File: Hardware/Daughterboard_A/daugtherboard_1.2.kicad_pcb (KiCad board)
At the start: 2 copper layers, 165.6 x 82.3 mm, 72 parts, among them J2 RJ45, J3 RJ45, J4 Conn_01x07, J5 Conn_01x04, J6 Conn_01x07, U1 IM66D132H, U16 TXS0108EPW, U17 LP5907MFX-1.8/NOPB, U2 IM66D132H, U3 IM66D132H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

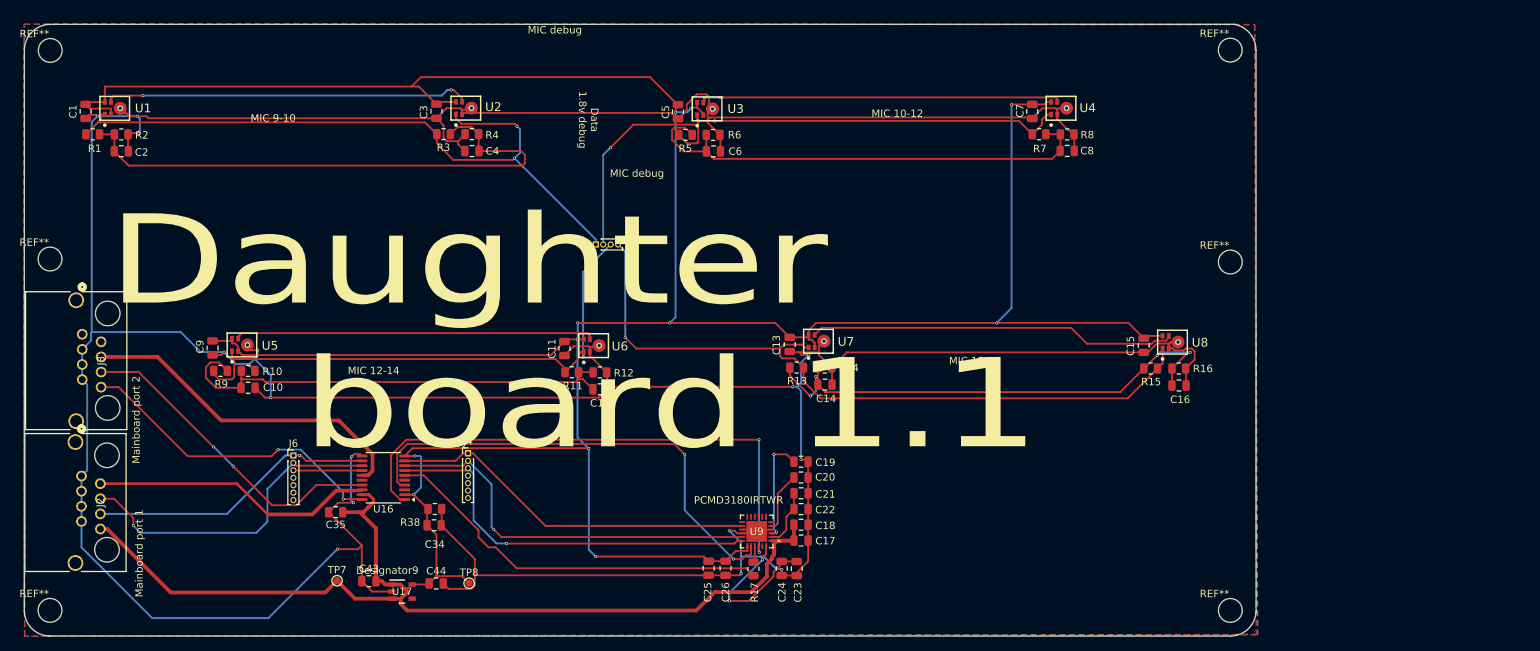
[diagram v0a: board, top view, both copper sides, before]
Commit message: implemented  ethernet port pcb R/a
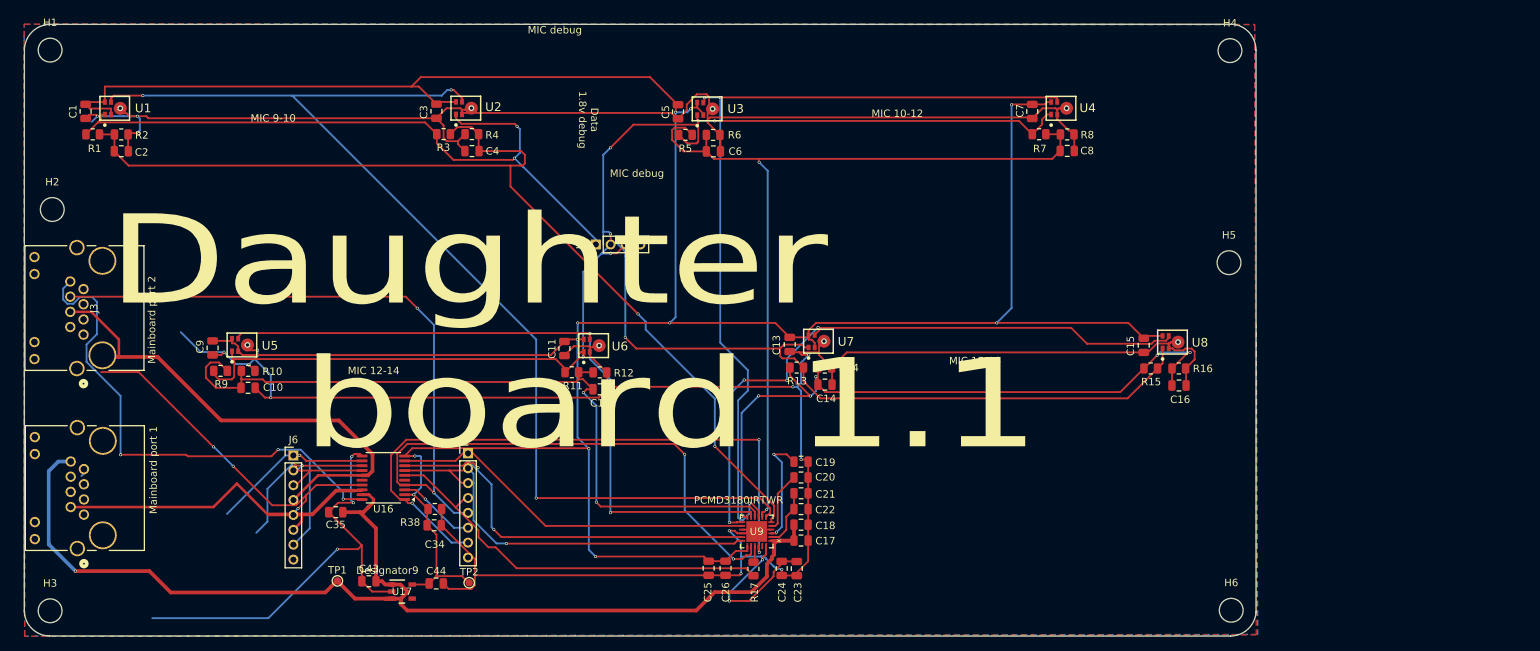
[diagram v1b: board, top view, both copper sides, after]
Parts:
- removed REF** (x6): MountingHole_3.2mm_M3, MountingHole:MountingHole_3.2mm_M3
- removed TP7, TP8: TestPoint, TestPoint:TestPoint_Pad_D1.0mm
- added H1: 3.2mm, MountingHole:MountingHole_3.2mm_M3_ISO14580, F.Cu at (46.8, 36.6)
- added H2: 3.2mm, MountingHole:MountingHole_3.2mm_M3_ISO14580, F.Cu at (47.0, 58.1)
- added H3: 3.2mm, MountingHole:MountingHole_3.2mm_M3_ISO14580, F.Cu at (46.8, 112.0)
- added H4: 3.2mm, MountingHole:MountingHole_3.2mm_M3_ISO14580, F.Cu at (205.4, 36.7)
- added H5: 3.2mm, MountingHole:MountingHole_3.2mm_M3_ISO14580, F.Cu at (205.2, 65.2)
- added H6: 3.2mm, MountingHole:MountingHole_3.2mm_M3_ISO14580, F.Cu at (205.6, 111.9)
- added TP1: TestPoint, TestPoint:TestPoint_Pad_D1.0mm, F.Cu at (85.4, 108.0)
- added TP2: TestPoint, TestPoint:TestPoint_Pad_D1.0mm, F.Cu at (103.1, 108.2)
- J2, J3: value RJ45 -> RJHSE5380; footprint RJHSE-3380:CONN_RJHSE-3380_AMP -> RJHSE-5380:RJHSE5380_AMP
- J4, J6: value Conn_01x07 -> Conn_01x08; footprint Connector_PinHeader_1.00mm:PinHeader_1x07_P1.00mm_Vertical -> Connector_PinHeader_2.00mm:PinHeader_1x08_P2.00mm_Vertical
- J5: footprint Connector_PinHeader_1.00mm:PinHeader_1x04_P1.00mm_Vertical -> Connector_PinHeader_2.00mm:PinHeader_1x04_P2.00mm_Vertical
- moved J2 1.61 mm to (51.4, 95.5)
- moved J3 0.18 mm to (51.2, 74.9)
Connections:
- C10 pad 1: micGRP_3out_1.8V -> micGRP_7out_1.8V
- C12 pad 1: micGRP_3out_1.8V -> micGRP_7out_1.8V
- C14 pad 1: micGRP_4out_1.8V -> micGRP_8out_1.8V
- C16 pad 1: micGRP_4out_1.8V -> micGRP_8out_1.8V
- C2 pad 1: micGRP_1out_1.8V -> micGRP_5out_1.8V
- C4 pad 1: micGRP_1out_1.8V -> micGRP_5out_1.8V
- C6 pad 1: micGRP_2out_1.8V -> micGRP_6out_1.8V
- C8 pad 1: micGRP_2out_1.8V -> micGRP_6out_1.8V
- J2 pad 10: (no net) -> GND
- J2 pad 9: (no net) -> unconnected-(J2-Pad9)
- J3 pad 1: unconnected-(J3-Pad1) -> GND
- J3 pad 10: (no net) -> GND
- J3 pad 2: unconnected-(J3-Pad2) -> SDA_SSZ_1.8V
- J3 pad 6: MCLK_TDM2_3.3V -> MCLK_TDM2_1.8V
- J3 pad 9: (no net) -> GND
- J4 pad 4: OUTPUT_TDM1_1.8V -> OUTPUT_TDM2_1.8V
- J4 pad 5: MCLK_TDM1_1.8V -> MCLK_TDM2_1.8V
- J4 pad 6: FSYNC_TDM1_1.8V -> FSYNC_TDM2_1.8V
- J4 pad 7: BCLK_TDM1_1.8V -> BCLK_TDM2_1.8V
- J6 pad 4: OUTPUT_TDM1_3.3V -> OUTPUT_TDM2_3.3V
- J6 pad 5: MCLK_TDM1_3.3V -> MCLK_TDM2_3.3V
- J6 pad 6: FSYNC_TDM1_3.3V -> FSYNC_TDM2_3.3V
- J6 pad 7: BCLK_TDM1_3.3V -> BCLK_TDM2_3.3V
- R1 pad 2: micGRP_1out_1.8V -> micGRP_5out_1.8V
- R10 pad 1: micGRP_3out_1.8V -> micGRP_7out_1.8V
- R11 pad 2: micGRP_3out_1.8V -> micGRP_7out_1.8V
- R12 pad 1: micGRP_3out_1.8V -> micGRP_7out_1.8V
- R13 pad 1: micGRP_4out_1.8V -> micGRP_8out_1.8V
- R14 pad 1: micGRP_4out_1.8V -> micGRP_8out_1.8V
- R15 pad 1: micGRP_4out_1.8V -> micGRP_8out_1.8V
- R16 pad 1: micGRP_4out_1.8V -> micGRP_8out_1.8V
- R2 pad 2: micGRP_1out_1.8V -> micGRP_5out_1.8V
- R3 pad 2: micGRP_1out_1.8V -> micGRP_5out_1.8V
- R4 pad 1: micGRP_1out_1.8V -> micGRP_5out_1.8V
- R5 pad 2: micGRP_2out_1.8V -> micGRP_6out_1.8V
- R6 pad 1: micGRP_2out_1.8V -> micGRP_6out_1.8V
- R7 pad 2: micGRP_2out_1.8V -> micGRP_6out_1.8V
- R8 pad 1: micGRP_2out_1.8V -> micGRP_6out_1.8V
- R9 pad 2: micGRP_3out_1.8V -> micGRP_7out_1.8V
- U1 pad 4: micgrp_1IN_1.8V -> micgrp_5IN_1.8V
- U2 pad 4: micgrp_1IN_1.8V -> micgrp_5IN_1.8V
- U3 pad 4: micGRP_2IN_1.8V -> micGRP_6IN_1.8V
- U4 pad 4: micGRP_2IN_1.8V -> micGRP_6IN_1.8V
- U5 pad 4: micGRP_3IN_1.8V -> micGRP_7IN_1.8V
- U6 pad 4: micGRP_3IN_1.8V -> micGRP_7IN_1.8V
- U7 pad 4: micGRP_4IN_1.8V -> micGRP_8IN_1.8V
- U8 pad 4: micGRP_4IN_1.8V -> micGRP_8IN_1.8V
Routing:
- net micgrp_5IN_1.8V: track 0.00 -> 150.4 mm, vias 0 -> 3
- net micGRP_5out_1.8V: track 0.00 -> 137.6 mm, vias 0 -> 2
- net micGRP_6out_1.8V: track 0.00 -> 114.9 mm, vias 0 -> 2
- net micGRP_6IN_1.8V: track 0.00 -> 113.3 mm, vias 0 -> 3
- net micGRP_7out_1.8V: track 0.00 -> 103.5 mm, vias 0 -> 2
- net micGRP_8out_1.8V: track 0.00 -> 93.9 mm, vias 0 -> 6
- net micGRP_7IN_1.8V: track 0.00 -> 93.7 mm, vias 0 -> 2
- net micGRP_8IN_1.8V: track 0.00 -> 86.7 mm, vias 0 -> 4
- net MCLK_TDM2_1.8V: track 65.4 -> 148.5 mm, vias 2 -> 4
- net GND: track 602.5 -> 519.8 mm
- net micGRP_1out_1.8V: track 74.8 -> 0.00 mm
- net micGRP_4out_1.8V: track 68.9 -> 0.00 mm, vias 4 -> 0
- net micGRP_2out_1.8V: track 64.7 -> 0.00 mm
- net micGRP_3out_1.8V: track 63.6 -> 0.00 mm
- net micGRP_4IN_1.8V: track 49.5 -> 0.00 mm
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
